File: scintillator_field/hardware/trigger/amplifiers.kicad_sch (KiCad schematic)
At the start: 5 parts, among them U6 OPA855xDSG, U7 TLV3501AIDBV

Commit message: conclude schematic
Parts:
- added C26, C27, C29, C30, C31, C33, C35, C36, C38, C39, C40, C42: 0.1u, Capacitor_SMD:C_0402_1005Metric, symbol Device:C
- added C28, C32, C37, C41: 2.2u, symbol Device:C
- added C34, C43, C44: 5p, Capacitor_SMD:C_0402_1005Metric, symbol Device:C
- added R19, R23, R27, R31: 49.9R, Resistor_SMD:R_0805_2012Metric_Pad1.20x1.40mm_HandSolder, symbol Device:R
- added R20, R24, R28, R32: 10k 0.1%, symbol Device:R
- added R25, R29, R33: 0, Resistor_SMD:R_0805_2012Metric_Pad1.20x1.40mm_HandSolder, symbol Device:R
- added R26, R30, R34: 226k 0.1%, symbol Device:R
- added U10, U6, U8: OPA855xDSG, Package_SON:WSON-8-1EP_2x2mm_P0.5mm_EP0.9x1.6mm, symbol opa855:OPA855xDSG
- added U11, U7, U9: TLV3501AIDBV, Package_TO_SOT_SMD:SOT-23-6, symbol tlv3501:TLV3501AIDBV
- C25: renamed from C37; footprint (none) -> Capacitor_SMD:C_0402_1005Metric
- U4: renamed from U6; symbol Amplifier_Operational:OPA855xDSG -> opa855:OPA855xDSG
- U5: renamed from U7; symbol Comparator:TLV3501AIDBV -> tlv3501:TLV3501AIDBV
- renumbered R16 to R21, R17 to R22
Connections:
- net VREF is gone; now on net AOUT1: U5.1 (-)
- net +3.8V: now also U10.4 (+), U6.4 (+), U8.4 (+)
- net +5V: now also C26.1, C27.1, C28.1, C30.1, C31.1, C32.1, C35.1, C36.1, C37.1, C39.1, C40.1, C41.1, U10.7 (V+), U10.8 (~{PD}), U11.4 (V+), U6.7 (V+), U6.8 (~{PD}), U7.4 (V+), U8.7 (V+), U8.8 (~{PD}), U9.4 (V+)
- net AOUT1: no longer U5.3 (+)
- net DOUT1: now also R20.2
- net GND: now also C26.2, C27.2, C28.2, C29.2, C30.2, C31.2, C32.2, C33.2, C35.2, C36.2, C37.2, C38.2, C39.2, C40.2, C41.2, C42.2, U10.5 (V-), U10.9 (V-), U11.2 (V-), U11.6 (SHDN), U6.5 (V-), U6.9 (V-), U7.2 (V-), U7.6 (SHDN), U8.5 (V-), U8.9 (V-), U9.2 (V-), U9.6 (SHDN)
- net at C25.2, R22.2, U4.1 (FB): no longer R21.1, U4.6
- new net: R27.1, R28.1, U9.3 (+)
- new net: R23.1, R24.1, U7.3 (+)
- new net: R31.1, R32.1, U11.3 (+)
- new net: C34.2, R26.2, U6.1 (FB)
- new net: R25.1, U6.6
- new net: R21.1, U4.6
- new net: R33.1, U10.6
- new net: R19.1, R20.1, U5.3 (+)
- new net: C43.2, R30.2, U8.1 (FB)
- new net: R29.1, U8.6
- new net: C44.2, R34.2, U10.1 (FB)
- new net +2.1V: C29.1, C33.1, C38.1, C42.1, R19.2, R23.2, R27.2, R31.2
- new net AOUT2: R25.2, U7.1 (-)
- new net AOUT3: R29.2, U9.1 (-)
- new net AOUT4: R33.2, U11.1 (-)
- new net DOUT2: R24.2, U7.5
- new net DOUT3: R28.2, U9.5
- new net DOUT4: R32.2, U11.5
- new net IN2: C34.1, R26.1, U6.3 (-)
- new net IN3: C43.1, R30.1, U8.3 (-)
- new net IN4: C44.1, R34.1, U10.3 (-)
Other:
- moved on the sheet: C25, R21, R22, U4, U5

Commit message: pcb v1
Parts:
- added C47, C48, C49, C50: 10n, Capacitor_SMD:C_0402_1005Metric, symbol Device:C
- C28, C32, C37, C41: footprint (none) -> Capacitor_SMD:C_0402_1005Metric
- C29, C33, C38, C42: value 0.1u -> 10n
- R19, R21, R23, R25, R27, R29, R31, R33: footprint Resistor_SMD:R_0805_2012Metric_Pad1.20x1.40mm_HandSolder -> Resistor_SMD:R_0402_1005Metric
- R20, R22, R24, R26, R28, R30, R32, R34: footprint (none) -> Resistor_SMD:R_0603_1608Metric
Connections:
- net +3.8V: now also C47.1, C48.1, C49.1, C50.1
- net GND: now also C47.2, C48.2, C49.2, C50.2

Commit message: pcb fabrication files
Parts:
- C25, C34, C43, C44: LCSC (none) -> C1573
- C26, C27, C30, C31, C35, C36, C39, C40: LCSC (none) -> C1581
- C28, C32, C37, C41: LCSC (none) -> C60078
- C29, C33, C38, C42, C47, C48, C49, C50: LCSC (none) -> C1524
- R19, R23, R27, R31: LCSC (none) -> C25120
- R20, R24, R28, R32: LCSC (none) -> C136139
- R21, R25, R29, R33: LCSC (none) -> C17168
- R22, R26, R30, R34: LCSC (none) -> C861233
- U10, U4, U6, U8: LCSC (none) -> C1409030
- U11, U5, U7, U9: LCSC (none) -> C193413

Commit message: fix trigger pcb
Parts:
- C25, C34, C43, C44: value 5p -> 3p; LCSC C1573 -> C1564
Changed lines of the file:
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@@
 			)
 		)
-		(property "Value" "5p"
+		(property "Value" "3p"
 			(at 66.04 51.308 0)
 			(effects
@@
 			)
 		)
-		(property "LCSC" "C1573"
+		(property "LCSC" "C1564"
 			(at 71.12 50.8 0)
 			(effects
@@
 			)
 		)
-		(property "Value" "5p"
+		(property "Value" "3p"
 			(at 66.04 173.228 0)
 			(effects
@@
 			)
 		)
-		(property "LCSC" "C1573"
+		(property "LCSC" "C1564"
 			(at 71.12 172.72 0)
 			(effects
@@
 			)
 		)
-		(property "Value" "5p"
+		(property "Value" "3p"
 			(at 66.04 132.588 0)
 			(effects
@@
 			)
 		)
-		(property "LCSC" "C1573"
+		(property "LCSC" "C1564"
 			(at 71.12 132.08 0)
 			(effects
@@
 			)
 		)
-		(property "Value" "5p"
+		(property "Value" "3p"
 			(at 66.04 91.948 0)
 			(effects
@@
 			)
 		)
-		(property "LCSC" "C1573"
+		(property "LCSC" "C1564"
 			(at 71.12 91.44 0)
 			(effects

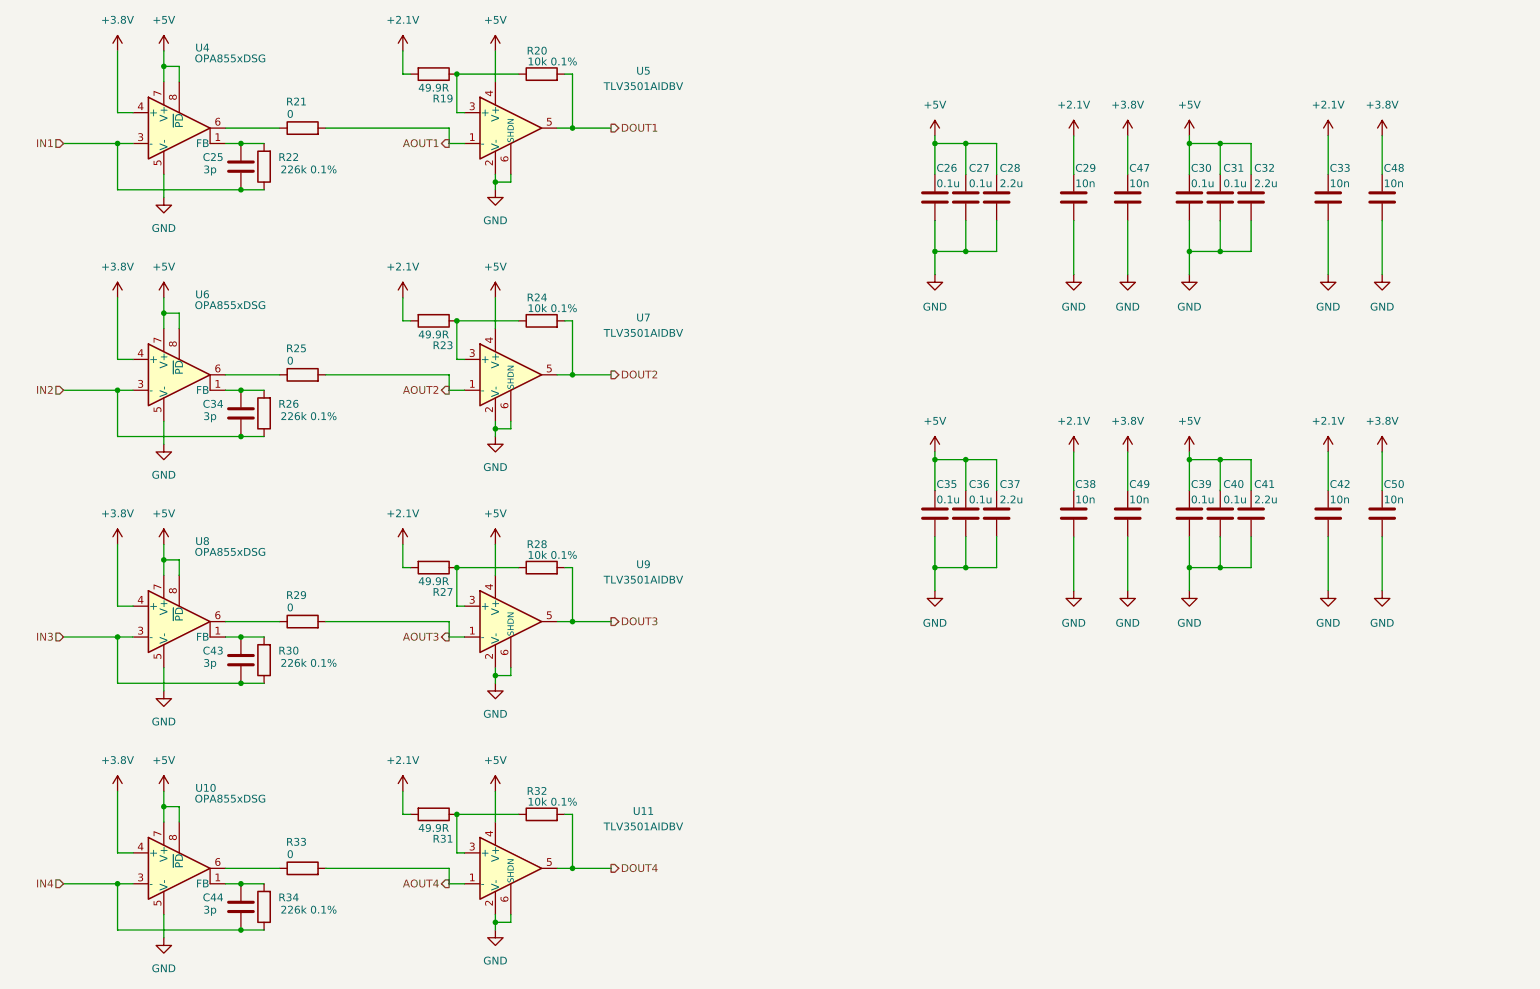
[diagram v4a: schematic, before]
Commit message: update to opa858
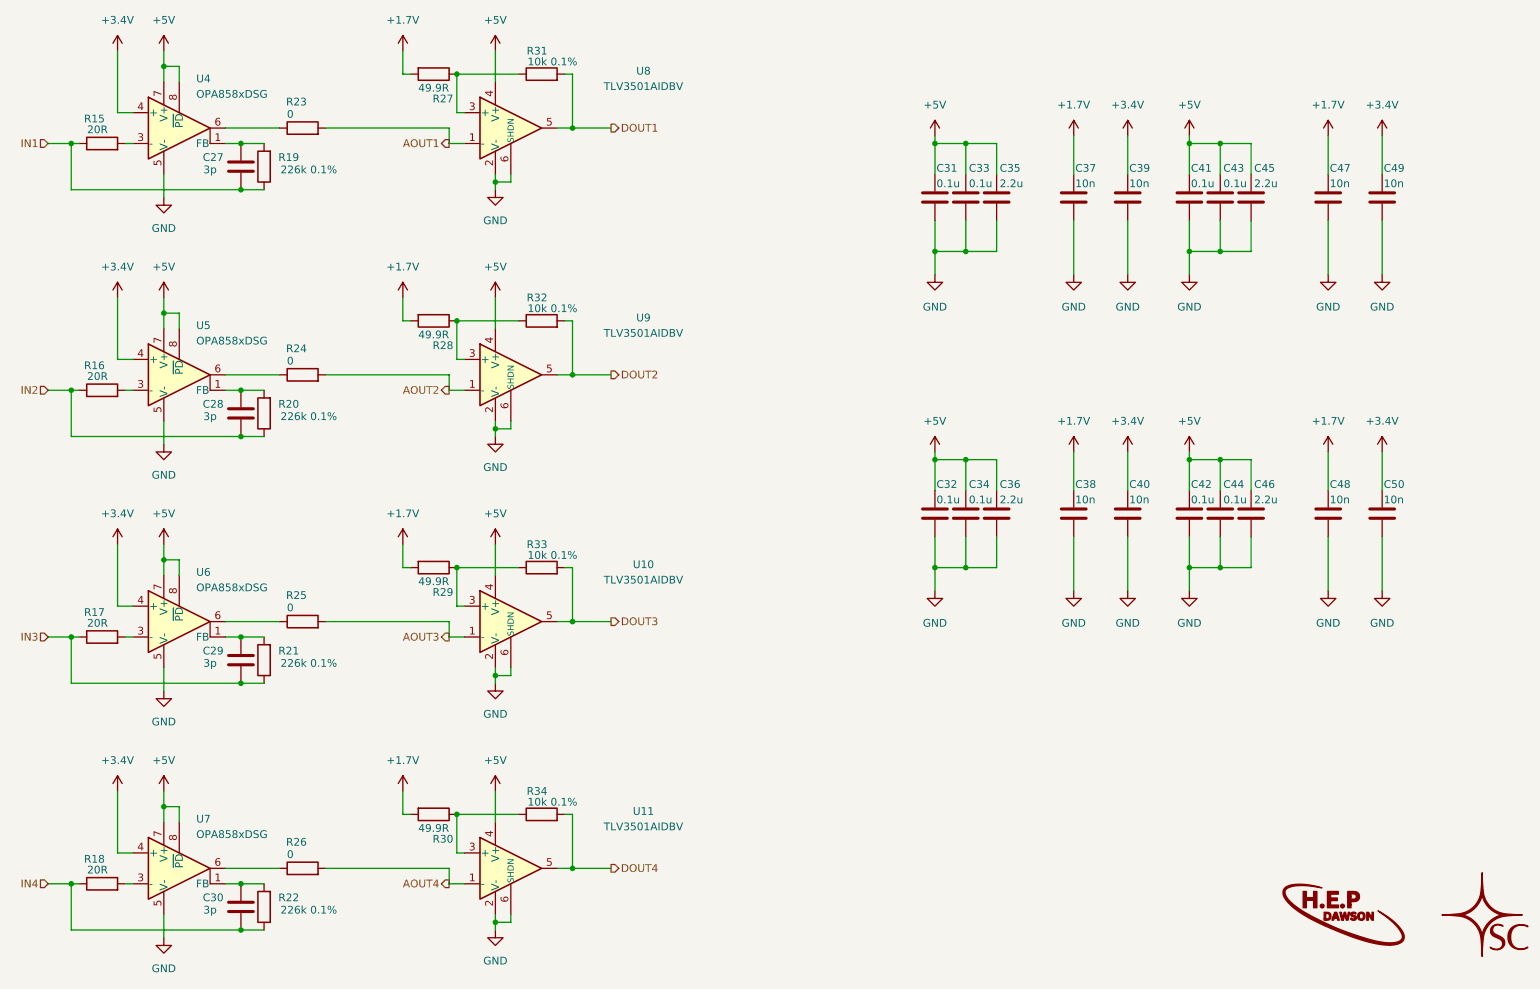
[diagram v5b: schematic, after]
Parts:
- removed C34, C43, C44: 3p, Capacitor_SMD:C_0402_1005Metric, symbol Device:C
- removed R26, R30, R34: 226k 0.1%, Resistor_SMD:R_0603_1608Metric, symbol Device:R
- removed U10, U4, U6, U8: OPA855xDSG, Package_SON:WSON-8-1EP_2x2mm_P0.5mm_EP0.9x1.6mm, symbol opa855:OPA855xDSG
- added C28, C29, C30: 3p, Capacitor_SMD:C_0402_1005Metric, symbol Device:C
- added R15, R16, R17, R18: 20R, Resistor_SMD:R_0402_1005Metric, symbol Device:R
- added R20, R21, R22: 226k 0.1%, Resistor_SMD:R_0603_1608Metric, symbol Device:R
- added U4, U5, U6, U7: OPA858xDSG, Package_SON:WSON-8-1EP_2x2mm_P0.5mm_EP0.9x1.6mm, symbol opa858:OPA858xDSG
- renumbered C25 to C27, C26 to C31, C35 to C32, C27 to C33, C36 to C34, C28 to C35, C37 to C36, C29 to C37, C47 to C39, C49 to C40, C30 to C41, C39 to C42, C31 to C43, C40 to C44, C32 to C45, C41 to C46, C33 to C47, C42 to C48, C48 to C49, R22 to R19, R21 to R23, R25 to R24, R29 to R25, R33 to R26, R19 to R27, R23 to R28, R27 to R29, R31 to R30, R20 to R31, R24 to R32, R28 to R33, R32 to R34, U9 to U10, U5 to U8, U7 to U9
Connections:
- net +5V: now also U4.7 (V+), U4.8 (~{PD}), U5.7 (V+), U5.8 (~{PD}), U6.7 (V+), U6.8 (~{PD}), U7.7 (V+), U7.8 (~{PD})
- net GND: now also U4.5 (V-), U4.9 (V-), U5.5 (V-), U5.9 (V-), U6.5 (V-), U6.9 (V-), U7.5 (V-), U7.9 (V-)
- net IN1: now also R15.1
- net IN2: now also C28.1, R16.1, R20.1
- net IN3: now also C29.1, R17.1, R21.1
- net IN4: now also C30.1, R18.1, R22.1
- net at R24.1: now also U5.6
- net at R23.1: now also U4.6
- net at C27.2, R19.2: now also U4.1 (FB)
- net at R26.1: now also U7.6
- net at R25.1: now also U6.6
- net +2.1V renamed +1.7V
- net +3.8V renamed +3.4V
- net +3.4V: now also U4.4 (+), U5.4 (+), U6.4 (+), U7.4 (+)
- new net: C29.2, R21.2, U6.1 (FB)
- new net: C30.2, R22.2, U7.1 (FB)
- new net: R15.2, U4.3 (-)
- new net: R18.2, U7.3 (-)
- new net: C28.2, R20.2, U5.1 (FB)
- new net: R17.2, U6.3 (-)
- new net: R16.2, U5.3 (-)
